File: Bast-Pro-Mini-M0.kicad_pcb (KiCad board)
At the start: 2 copper layers, 17.8 x 33 mm, 23 parts, among them J1 USB_B_Micro, J2 Conn_02x02_Odd_Even, P1 Digital, P2 ADC, P4 Analog, SW1 SW_DPST_x2, U1 AP2112K-3.3TRG1, U2 ATSAMD21E18A-AF

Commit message: first design
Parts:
- moved C5 2.63 mm to (150.4, 111.2), turned to 180 degrees
- moved C4 0.70 mm to (150.3, 108.7)
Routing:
- net +3V3: track 20.8 -> 65.0 mm
- net /RESET: track 3.85 -> 37.9 mm, vias 0 -> 3
- net GND: track 62.8 -> 85.5 mm, vias 3 -> 8
- net /4: track 0.00 -> 22.2 mm, vias 0 -> 3
- net /SWDIO: track 5.19 -> 18.1 mm, vias 1 -> 3
- net /3(**): track 0.00 -> 12.7 mm, vias 0 -> 1
- net /SWCLK: track 4.86 -> 10.8 mm
- net /1(Tx): track 34.9 -> 31.7 mm
- net /0(Rx): track 34.0 -> 30.8 mm
- net Net-(C4-Pad1): track 0.00 -> 3.01 mm
- net /11(**/MOSI): track 24.8 -> 22.2 mm
- net /8: track 23.7 -> 26.2 mm
- net /A0: track 5.71 -> 8.04 mm, vias 0 -> 1
- net /7: track 17.3 -> 19.6 mm
- net /A3: track 20.4 -> 18.7 mm
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- added copper zone on B.Cu, net GND
- added copper zone on F.Cu, net GND
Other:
- rule trace_min: 0.2 -> 0.3

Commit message: Bast Pro Mini (ultimate revision)
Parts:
- moved R2 0.29 mm to (141.5, 89.5)
- moved D2 0.25 mm to (143.2, 89.7)
- moved C3 0.21 mm to (145.5, 95.9)
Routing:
- net /4: track 22.2 -> 42.9 mm, vias 3 -> 6
- net /D+: track 27.7 -> 29.5 mm
- net /D-: track 28.1 -> 27.4 mm
- net +3V3: track 65.0 -> 65.7 mm

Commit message: Bast Pro Mini (utimate revision) (Now yes)
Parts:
- G***: moved to B.Cu
- moved REF*** 60.9 mm to (150.2, 109.3)
- moved G*** 49.9 mm to (143.8, 93.8)
- moved G*** 35.0 mm to (143.1, 108.0), turned to 180 degrees
- moved G*** 34.2 mm to (146.5, 93.4)
- moved G*** 32.6 mm to (142.4, 91.5)
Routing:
- net GND: track 85.4 -> 90.1 mm
- net /SWDIO: track 18.1 -> 18.9 mm

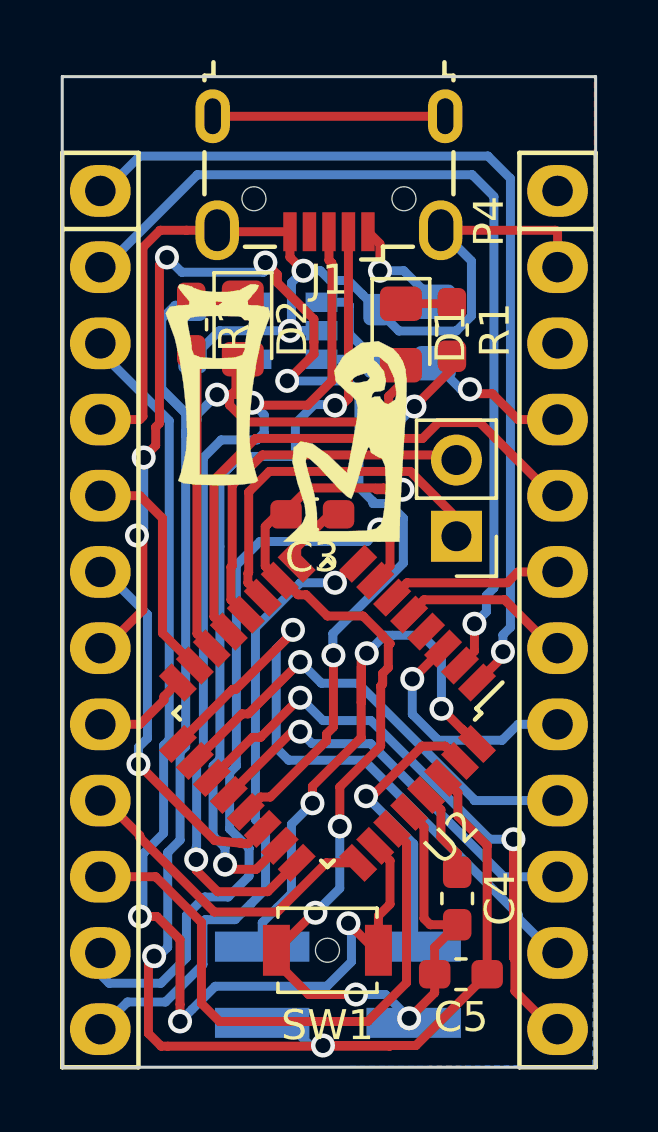
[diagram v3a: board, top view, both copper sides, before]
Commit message: Bast Pro Mini M0 add 3d model usb
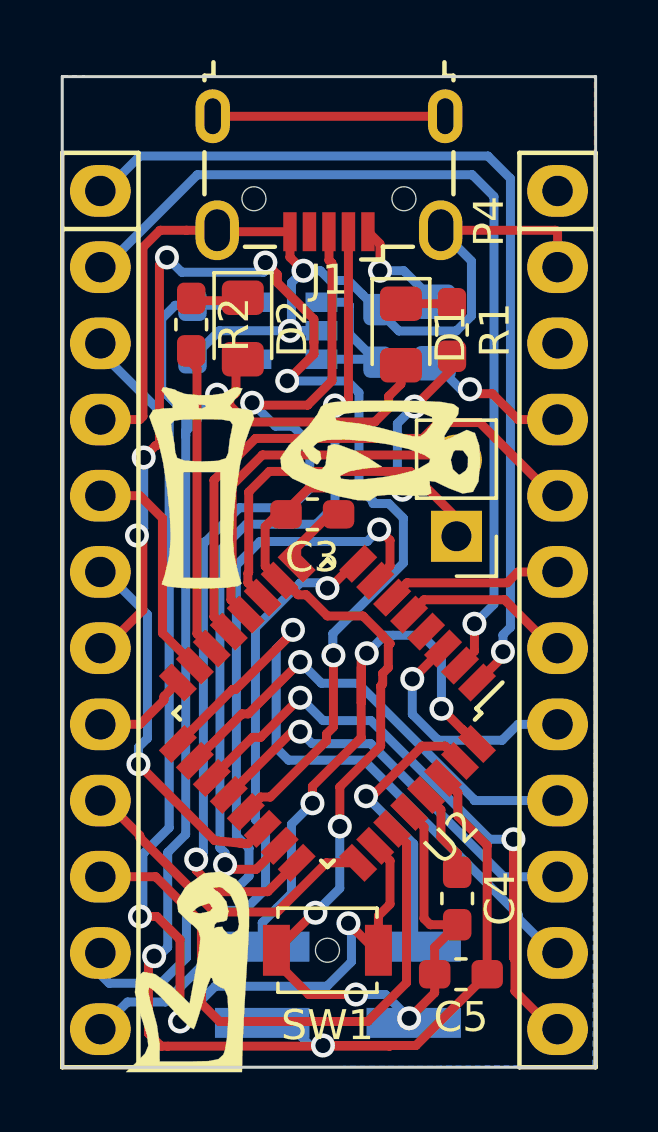
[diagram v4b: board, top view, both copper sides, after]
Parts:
- removed the G*** at (143.1, 108.0)
- removed the G*** at (146.5, 93.4)
- added G***: LOGO, LOGO, F.Cu at (147.7, 93.7)
- added G***: LOGO, LOGO, F.Cu at (141.3, 111.1)
- moved G*** 12.0 mm to (143.2, 105.8)
- moved REF*** 3.70 mm to (149.8, 105.6)
- moved G*** 3.48 mm to (141.8, 95.0)
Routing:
- net /D+: track 29.5 -> 31.4 mm
- net /D-: track 27.4 -> 26.3 mm
